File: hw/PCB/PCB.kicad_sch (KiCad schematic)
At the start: 208 parts, among them IC1 SN74HC251PWR, IC2 SN74LV138APWR, IC3 SN74HC251PWR, K1 KEYSW, K10 KEYSW, K11 KEYSW, K12 KEYSW, K13 KEYSW, K14 KEYSW, K16 KEYSW, K17 KEYSW, K18 KEYSW, K19 KEYSW, K2 KEYSW, K20 KEYSW, K21 KEYSW, K22 KEYSW, K23 KEYSW, K24 KEYSW, K25 KEYSW, K26 KEYSW, K27 KEYSW, K28 KEYSW, K29 KEYSW, K3 KEYSW, K31 KEYSW, K32 KEYSW, K33 KEYSW, K34 KEYSW, K35 KEYSW, K36 KEYSW, K37 KEYSW, K38 KEYSW, K39 KEYSW, K4 KEYSW, K40 KEYSW, K41 KEYSW, K42 KEYSW, K43 KEYSW, K44 KEYSW, K46 KEYSW, K47 KEYSW, K48 KEYSW, K49 KEYSW, K5 KEYSW, K50 KEYSW, K51 KEYSW, K52 KEYSW, K53 KEYSW, K54 KEYSW, K55 KEYSW, K56 KEYSW, K57 KEYSW, K58 KEYSW, K59 KEYSW, K6 KEYSW, K61 KEYSW, K62 KEYSW, K63 KEYSW, K64 KEYSW, K65 KEYSW, K66 KEYSW, K67 KEYSW, K68 KEYSW, K69 KEYSW, K7 KEYSW, K8 KEYSW, K9 KEYSW, U1 TXB0108DQSR, U6 STM32L552ZETxQ

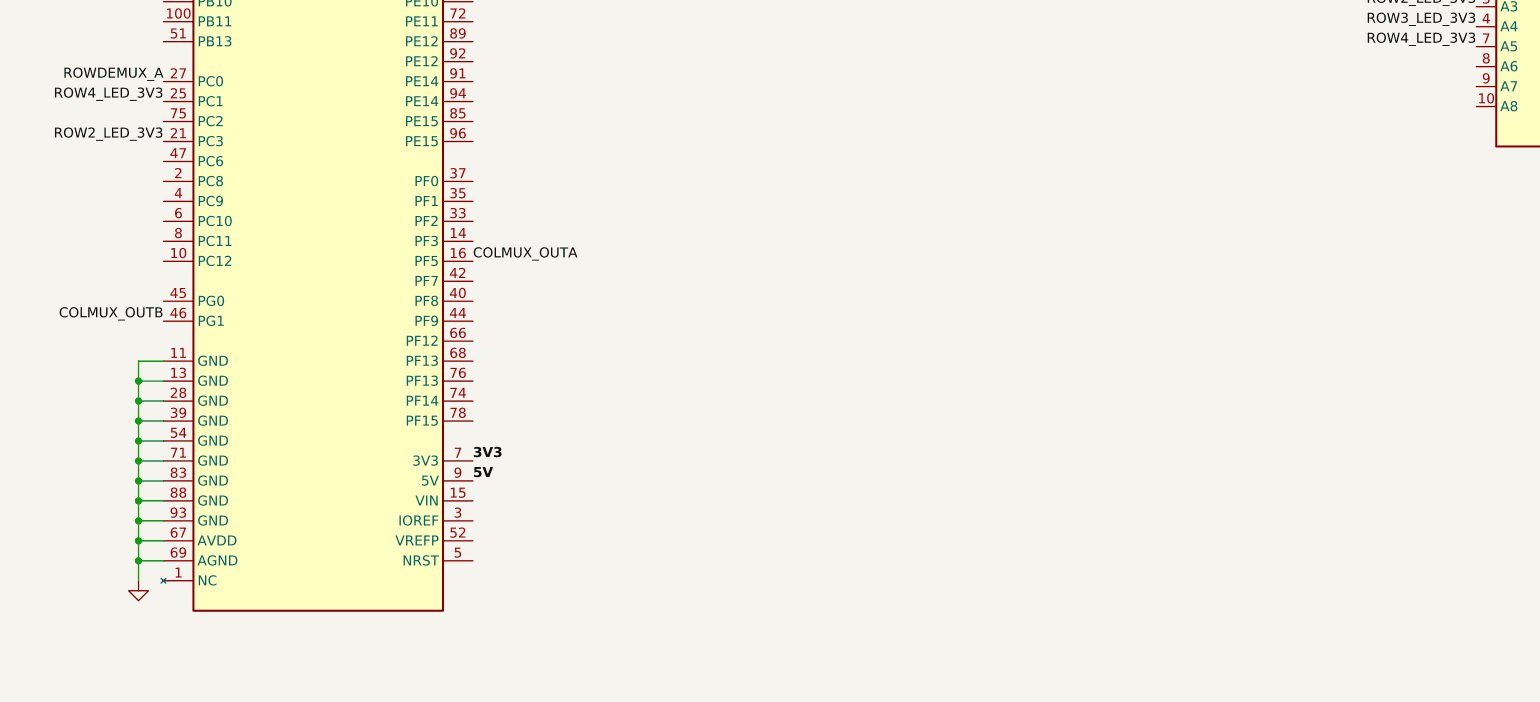
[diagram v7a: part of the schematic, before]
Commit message: Added basic test program for key matrix
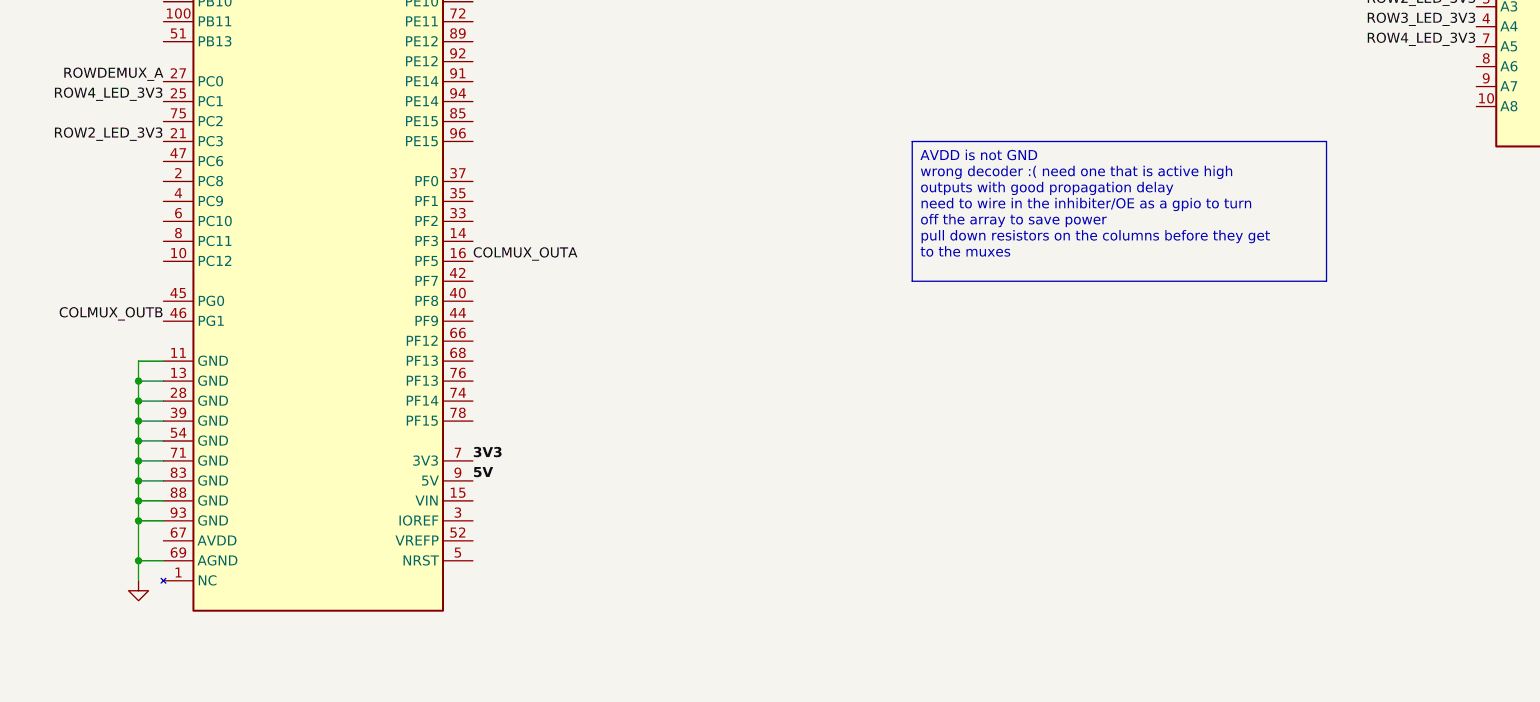
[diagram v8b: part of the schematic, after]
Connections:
- net GND: no longer U6.67 (AVDD)
